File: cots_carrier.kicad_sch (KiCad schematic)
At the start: 12 parts, among them J1 XT30PW-F, J2 XT30PW-M, U1 COTS Charger, U2 COTS LM2596 Buck

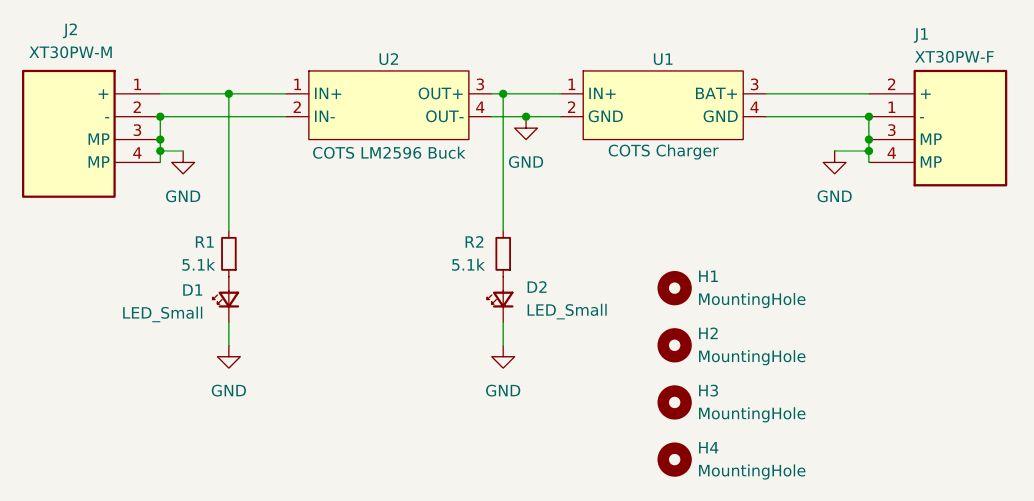
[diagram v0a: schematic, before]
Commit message: aircraft carrier silk screen
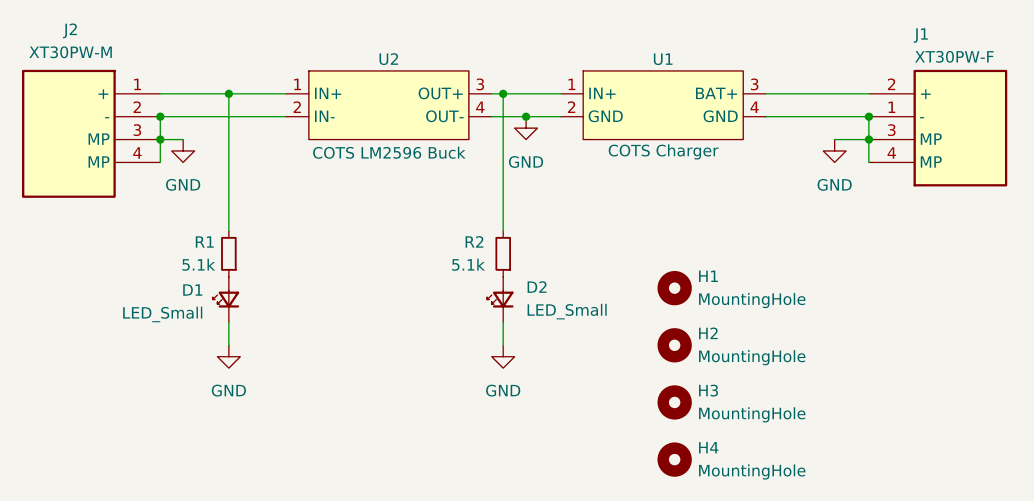
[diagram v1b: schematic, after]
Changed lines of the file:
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@@
-	)
-	(junction
-		(at 121.92 102.87)
-		(diameter 0)
-		(color 0 0 0 0)
 	)
 	(junction
@@
 	)
 	(junction
-		(at 200.66 102.87)
-		(diameter 0)
-		(color 0 0 0 0)
-	)
-	(junction
 		(at 200.66 99.06)
 		(diameter 0)
@@
 	(wire
 		(pts
-			(xy 121.92 102.87) (xy 121.92 104.14)
-		)
-		(stroke
-			(width 0)
-			(type default)
-		)
-	)
-	(wire
-		(pts
-			(xy 121.92 101.6) (xy 121.92 102.87)
-		)
-		(stroke
-			(width 0)
-			(type default)
-		)
-	)
-	(wire
-		(pts
-			(xy 196.85 102.87) (xy 200.66 102.87)
+			(xy 121.92 101.6) (xy 121.92 104.14)
+		)
+		(stroke
+			(width 0)
+			(type default)
+		)
+	)
+	(wire
+		(pts
+			(xy 196.85 101.6) (xy 200.66 101.6)
 		)
 		(stroke
@@
 	(wire
 		(pts
-			(xy 200.66 102.87) (xy 200.66 104.14)
-		)
-		(stroke
-			(width 0)
-			(type default)
-		)
-	)
-	(wire
-		(pts
 			(xy 189.23 96.52) (xy 200.66 96.52)
 		)
@@
 	(wire
 		(pts
-			(xy 121.92 102.87) (xy 124.46 102.87)
+			(xy 121.92 101.6) (xy 124.46 101.6)
 		)
 		(stroke
@@
 	(wire
 		(pts
-			(xy 200.66 101.6) (xy 200.66 102.87)
+			(xy 200.66 101.6) (xy 200.66 104.14)
 		)
 		(stroke
@@
 	(symbol
 		(lib_id "power:GND")
-		(at 124.46 102.87 0)
+		(at 124.46 101.6 0)
 		(unit 1)
 		(exclude_from_sim no)
@@
 		(fields_autoplaced yes)
 		(property "Reference" "#PWR02"
-			(at 124.46 109.22 0)
+			(at 124.46 107.95 0)
 			(effects
 				(font
@@
 		)
 		(property "Value" "GND"
-			(at 124.46 107.95 0)
+			(at 124.46 106.68 0)
 			(effects
 				(font
@@
 		)
 		(property "Footprint" ""
-			(at 124.46 102.87 0)
+			(at 124.46 101.6 0)
 			(effects
 				(font
@@
 		)
 		(property "Datasheet" ""
-			(at 124.46 102.87 0)
+			(at 124.46 101.6 0)
 			(effects
 				(font
@@
 		)
 		(property "Description" "Power symbol creates a global label with name \"GND\" , ground"
-			(at 124.46 102.87 0)
+			(at 124.46 101.6 0)
 			(effects
 				(font
@@
 	(symbol
 		(lib_id "power:GND")
-		(at 196.85 102.87 0)
+		(at 196.85 101.6 0)
 		(unit 1)
 		(exclude_from_sim no)
@@
 		(fields_autoplaced yes)
 		(property "Reference" "#PWR01"
-			(at 196.85 109.22 0)
+			(at 196.85 107.95 0)
 			(effects
 				(font
@@
 		)
 		(property "Value" "GND"
-			(at 196.85 107.95 0)
+			(at 196.85 106.68 0)
 			(effects
 				(font
@@
 		)
 		(property "Footprint" ""
-			(at 196.85 102.87 0)
+			(at 196.85 101.6 0)
 			(effects
 				(font
@@
 		)
 		(property "Datasheet" ""
-			(at 196.85 102.87 0)
+			(at 196.85 101.6 0)
 			(effects
 				(font
@@
 		)
 		(property "Description" "Power symbol creates a global label with name \"GND\" , ground"
-			(at 196.85 102.87 0)
-			(effects
-				(font
+			(at 196.85 101.6 0)
+			(effects
+				(font
